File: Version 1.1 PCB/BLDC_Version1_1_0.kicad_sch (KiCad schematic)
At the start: 14 parts, among them U1 ESP32-S3-WROOM-1

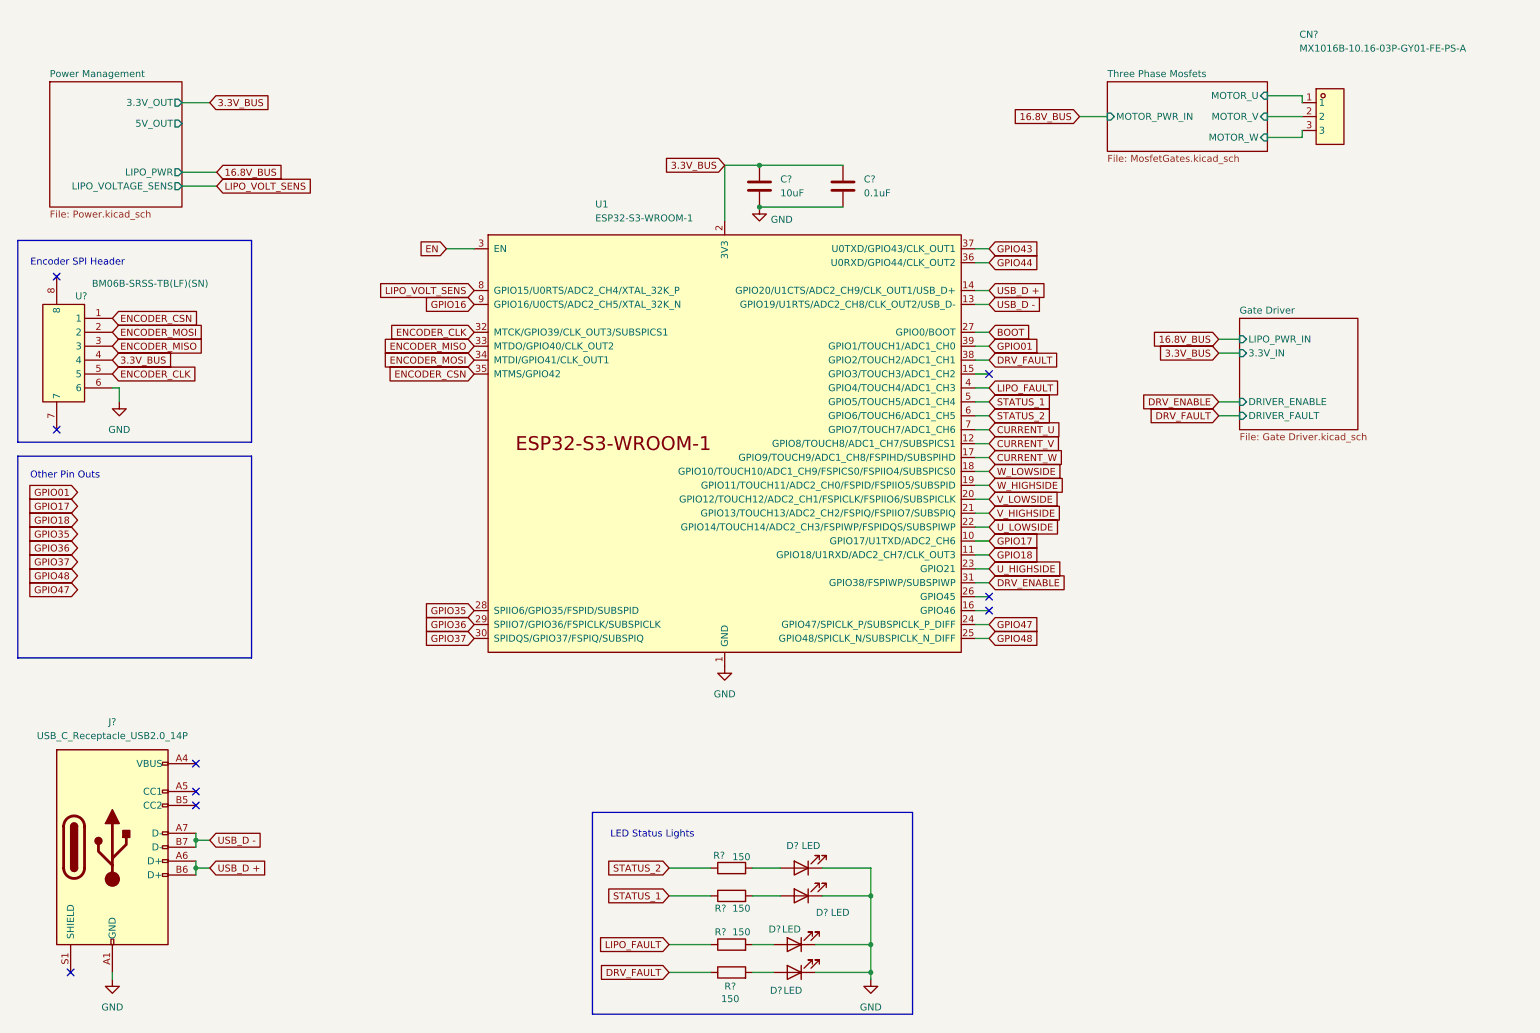
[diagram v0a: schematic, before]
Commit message: Added pins
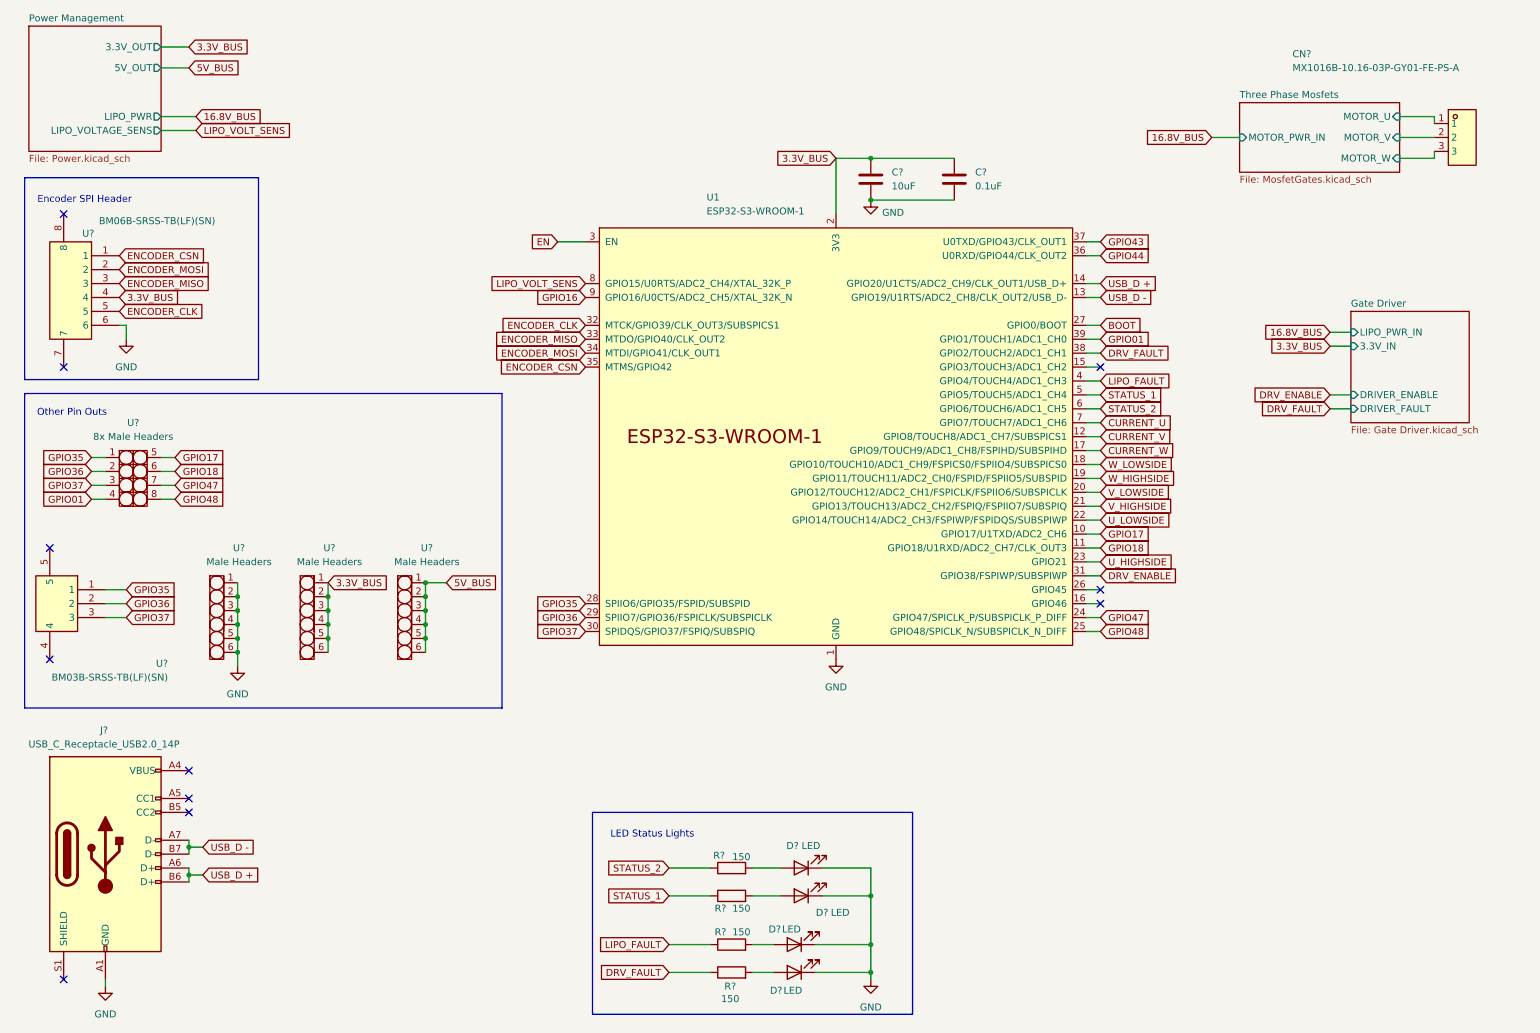
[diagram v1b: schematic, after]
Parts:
- added U?: BM03B-SRSS-TB(LF)(SN), easyeda2kicad:CONN-SMD-3P-P1.00_BM03B-SRSS-TB-LF-SN, symbol easyeda2kicad:BM03B-SRSS-TB(LF)(SN)
- added U? (x3): Male Headers, Project_BLDC_Foorprint_Library:1x6 Male Headers, symbol BLDC_Project_Sym_Lib:1x6_Male_Headers
- added U?: 8x Male Headers, Project_BLDC_Foorprint_Library:2x4 Male Headers, symbol BLDC_Project_Sym_Lib:2x4_Male_Headers
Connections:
- net 3.3V_BUS: now also U?.1, U?.2, U?.3, U?.4, U?.5, U?.6
- net GND: now also U?.1, U?.2, U?.3, U?.4, U?.5, U?.6
- net GPIO01: now also U?.4
- net GPIO17: now also U?.5
- net GPIO18: now also U?.6
- net GPIO35: now also U?.1, U?.1
- net GPIO36: now also U?.2, U?.2
- net GPIO37: now also U?.3, U?.3
- net GPIO47: now also U?.7
- net GPIO48: now also U?.8
- new net 5V_BUS: U?.1, U?.2, U?.3, U?.4, U?.5, U?.6
- no-connect marks 9 -> 11
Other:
- moved on the sheet: C?, CN?, J?, U1, U?

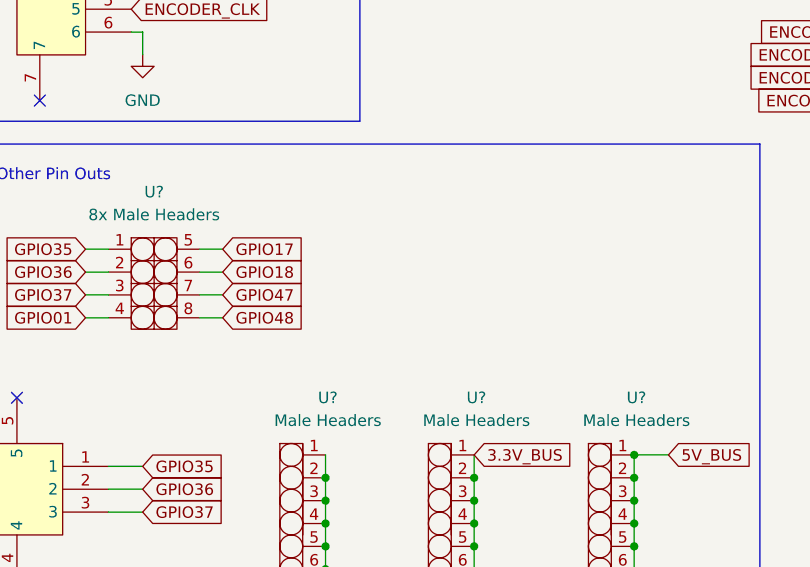
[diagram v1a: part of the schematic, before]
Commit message: Added soft starter to PCB
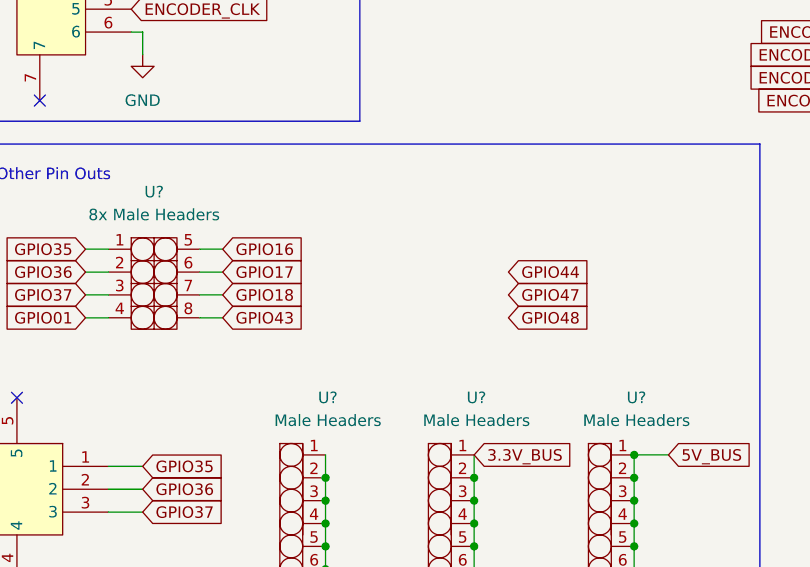
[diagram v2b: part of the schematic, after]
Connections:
- net GPIO16: now also U?.5
- net GPIO17: now also U?.6; no longer U?.5
- net GPIO18: now also U?.7; no longer U?.6
- net GPIO43: now also U?.8
- net GPIO47: no longer U?.7
- net GPIO48: no longer U?.8

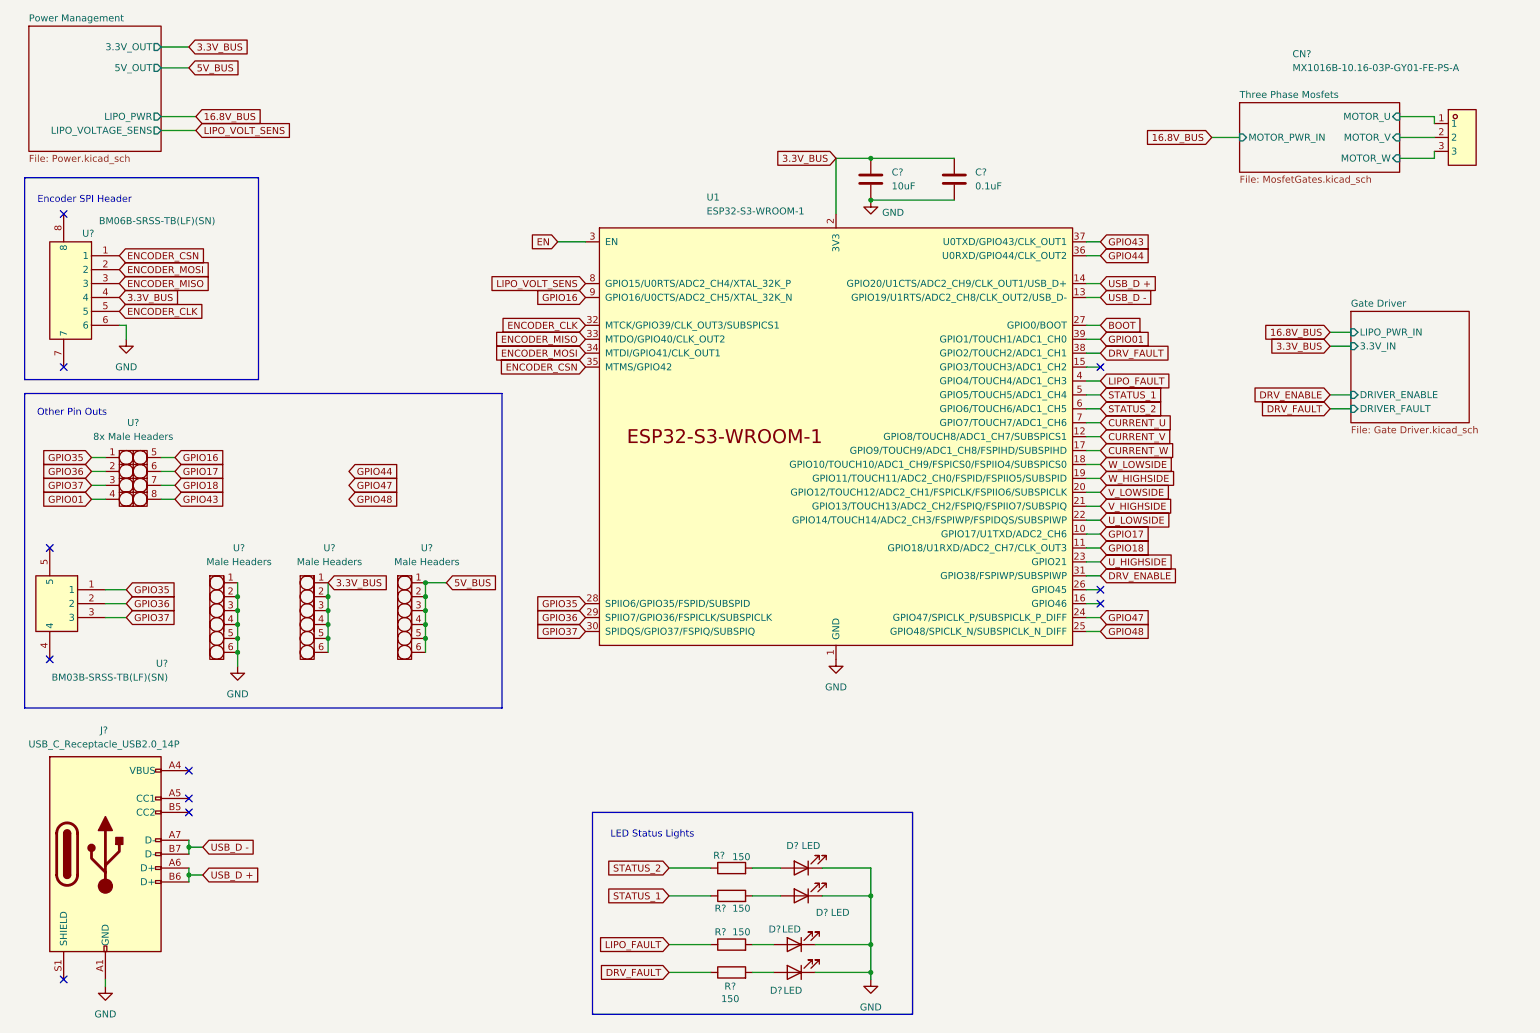
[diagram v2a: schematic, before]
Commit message: Added ESD protection and test pins
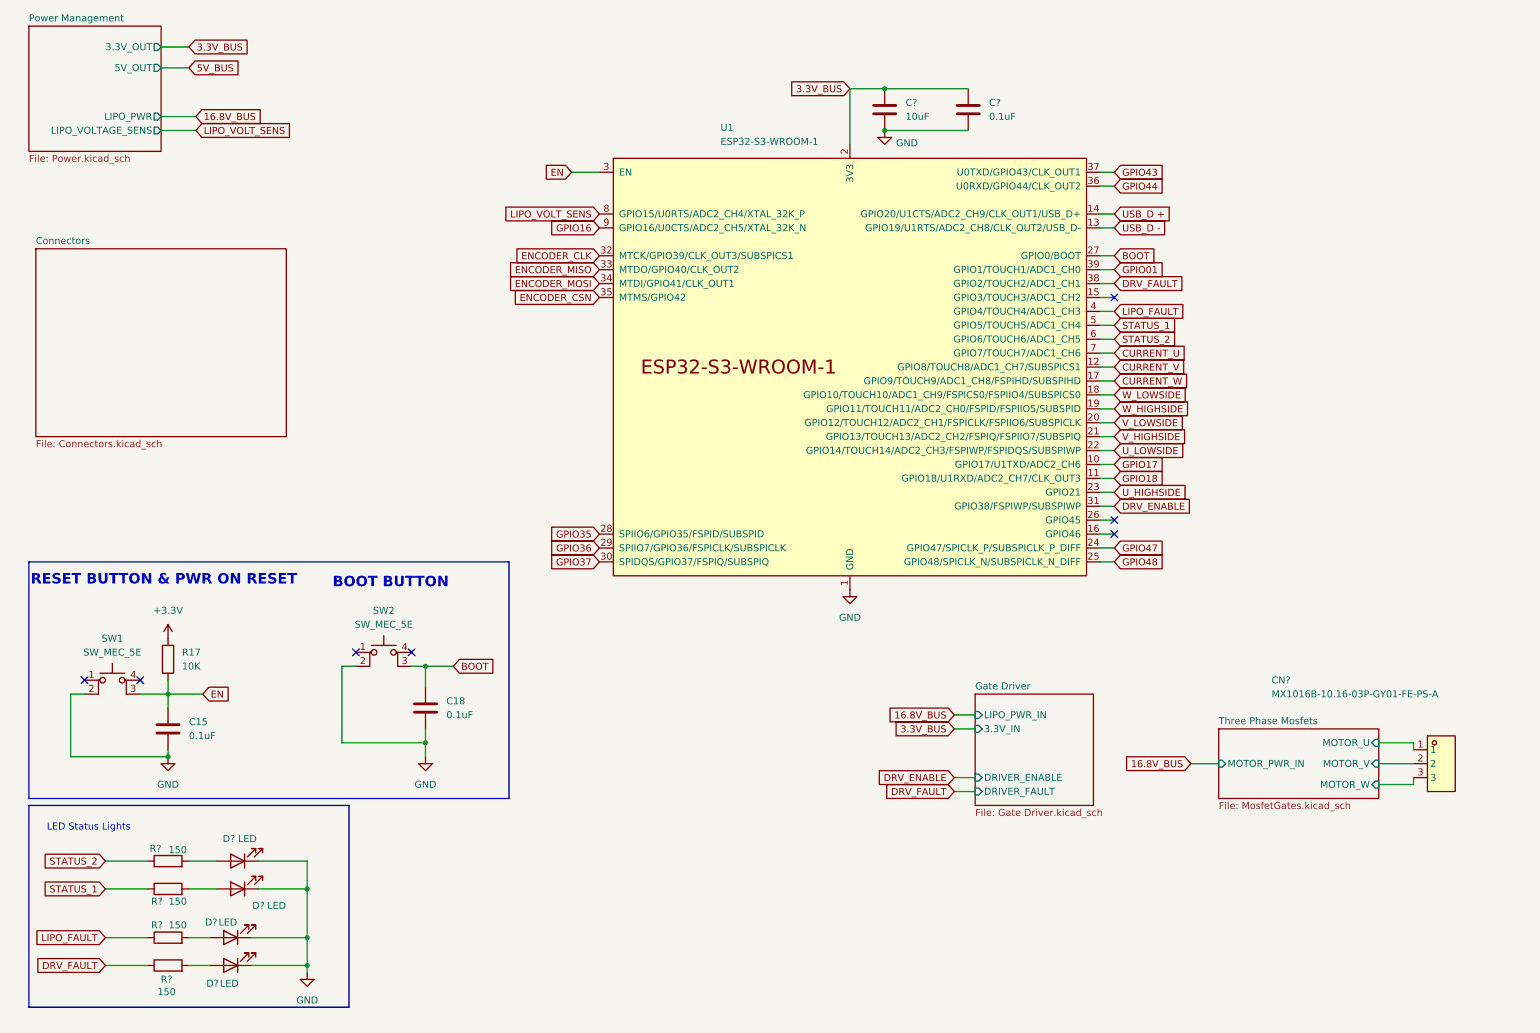
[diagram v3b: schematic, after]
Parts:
- removed J?: USB_C_Receptacle_USB2.0_14P, symbol Connector:USB_C_Receptacle_USB2.0_14P
- removed U?: BM03B-SRSS-TB(LF)(SN), easyeda2kicad:CONN-SMD-3P-P1.00_BM03B-SRSS-TB-LF-SN, symbol easyeda2kicad:BM03B-SRSS-TB(LF)(SN)
- removed U?: BM06B-SRSS-TB(LF)(SN), easyeda2kicad:CONN-SMD-6P-P1.00_BM06B-SRSS-TB-LF-SN, symbol easyeda2kicad:BM06B-SRSS-TB(LF)(SN)
- removed U? (x3): Male Headers, Project_BLDC_Foorprint_Library:1x6 Male Headers, symbol BLDC_Project_Sym_Lib:1x6_Male_Headers
- removed U?: 8x Male Headers, Project_BLDC_Foorprint_Library:2x4 Male Headers, symbol BLDC_Project_Sym_Lib:2x4_Male_Headers
- added C15, C18: 0.1uF, Capacitor_SMD:C_0805_2012Metric_Pad1.18x1.45mm_HandSolder, symbol Device:C
- added R17: 10K, Resistor_SMD:R_0805_2012Metric_Pad1.20x1.40mm_HandSolder, symbol Device:R
- added SW1, SW2: SW_MEC_5E, easyeda2kicad:SW-SMD_4P-L5.2-W5.2-P3.70-LS6.5, symbol Switch:SW_MEC_5E
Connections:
- net BOOT: now also C18.1, SW2.3 (K)
- net EN: now also C15.1, R17.2, SW1.3 (K)
- net GND: now also C15.2, C18.2, SW1.2, SW2.2
- new net +3.3V: R17.1
- no-connect marks 11 -> 7
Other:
- added sheet Connectors (Connectors.kicad_sch)
- note added: "BOOT BUTTON"
- note added: "RESET BUTTON & PWR ON RESET"
- note removed: "Encoder SPI Header"
- note removed: "Other Pin Outs"
- moved on the sheet: C?, CN?, D?, R?, U1

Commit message: began part placement
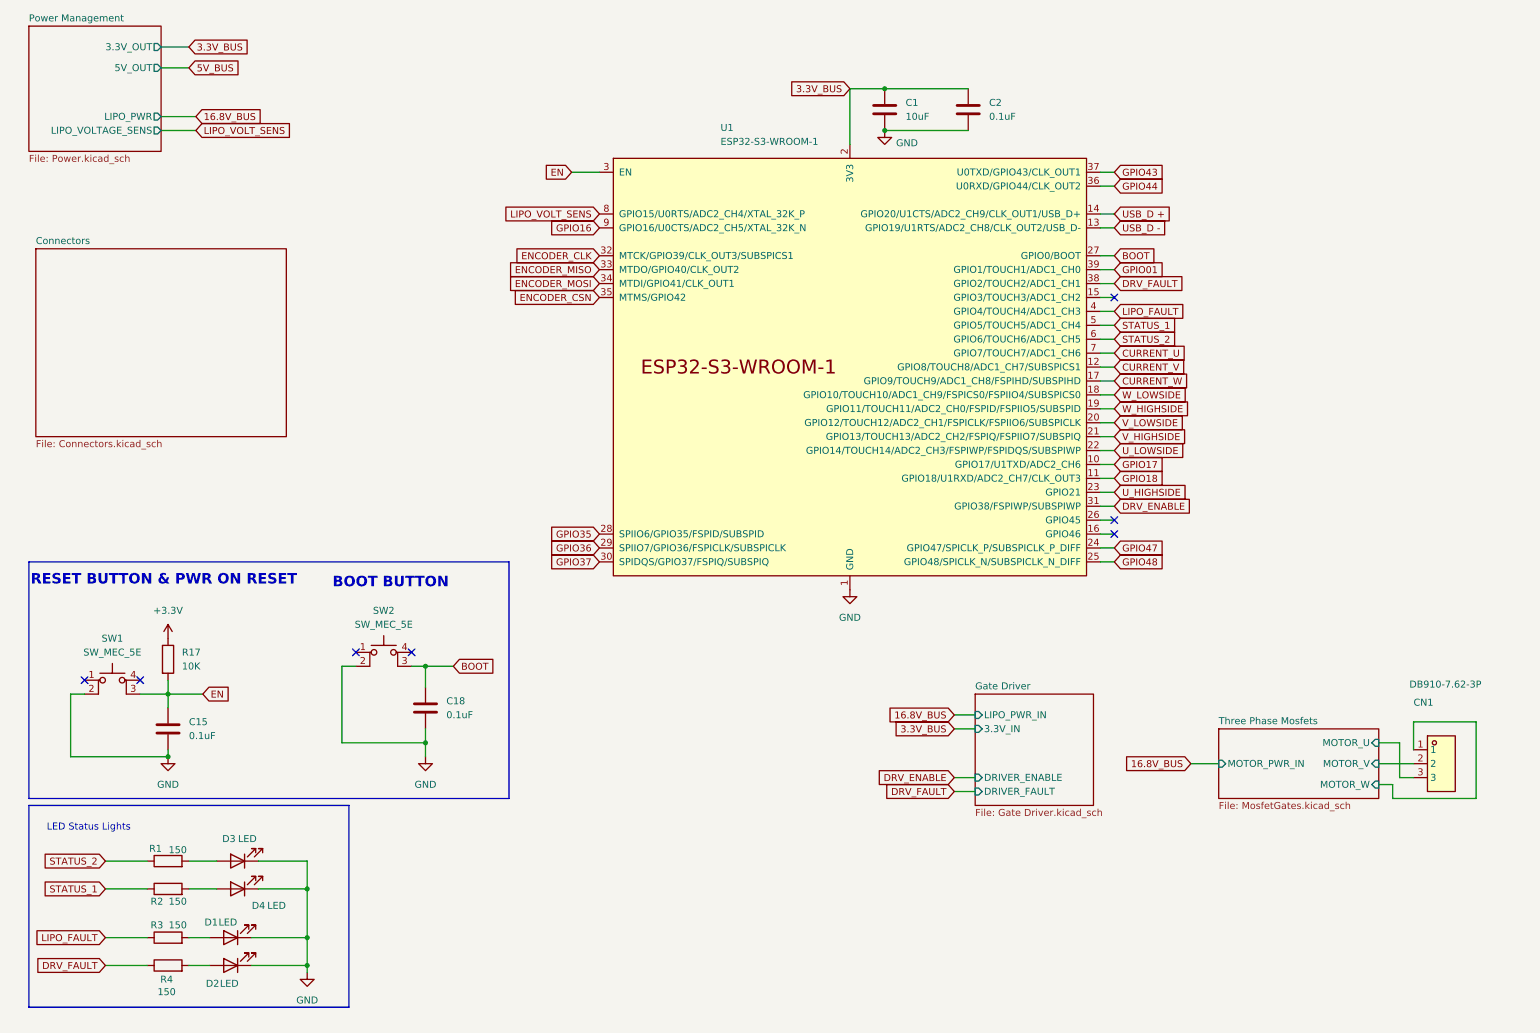
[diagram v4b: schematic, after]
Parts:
- removed CN?: MX1016B-10.16-03P-GY01-FE-PS-A, easyeda2kicad:CONN-TH_MX1016B-10.16-03P-GY01-FE-PS-A, symbol easyeda2kicad:MX1016B-10.16-03P-GY01-FE-PS-A
- added CN1: DB910-7.62-3P, easyeda2kicad:CONN-TH_3P-P7.62_DB910-7.62-3P, symbol easyeda2kicad:DB910-7.62-3P
- C1, C2: renamed from C?; footprint (none) -> Capacitor_SMD:C_0805_2012Metric_Pad1.18x1.45mm_HandSolder
- D1, D2: renamed from D?; footprint (none) -> LED_SMD:LED_0603_1608Metric_Pad1.05x0.95mm_HandSolder
- D3, D4: renamed from D?; footprint (none) -> LED_SMD:LED_0805_2012Metric_Pad1.15x1.40mm_HandSolder
- R1, R2, R3, R4: renamed from R?; footprint (none) -> Resistor_SMD:R_0805_2012Metric_Pad1.20x1.40mm_HandSolder
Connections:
- net Three Phase Mosfets/MOTOR_U: now also CN1.3
- net Three Phase Mosfets/MOTOR_V: now also CN1.2
- net Three Phase Mosfets/MOTOR_W: now also CN1.1
